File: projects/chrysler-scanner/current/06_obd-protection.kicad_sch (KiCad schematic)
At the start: 11 parts

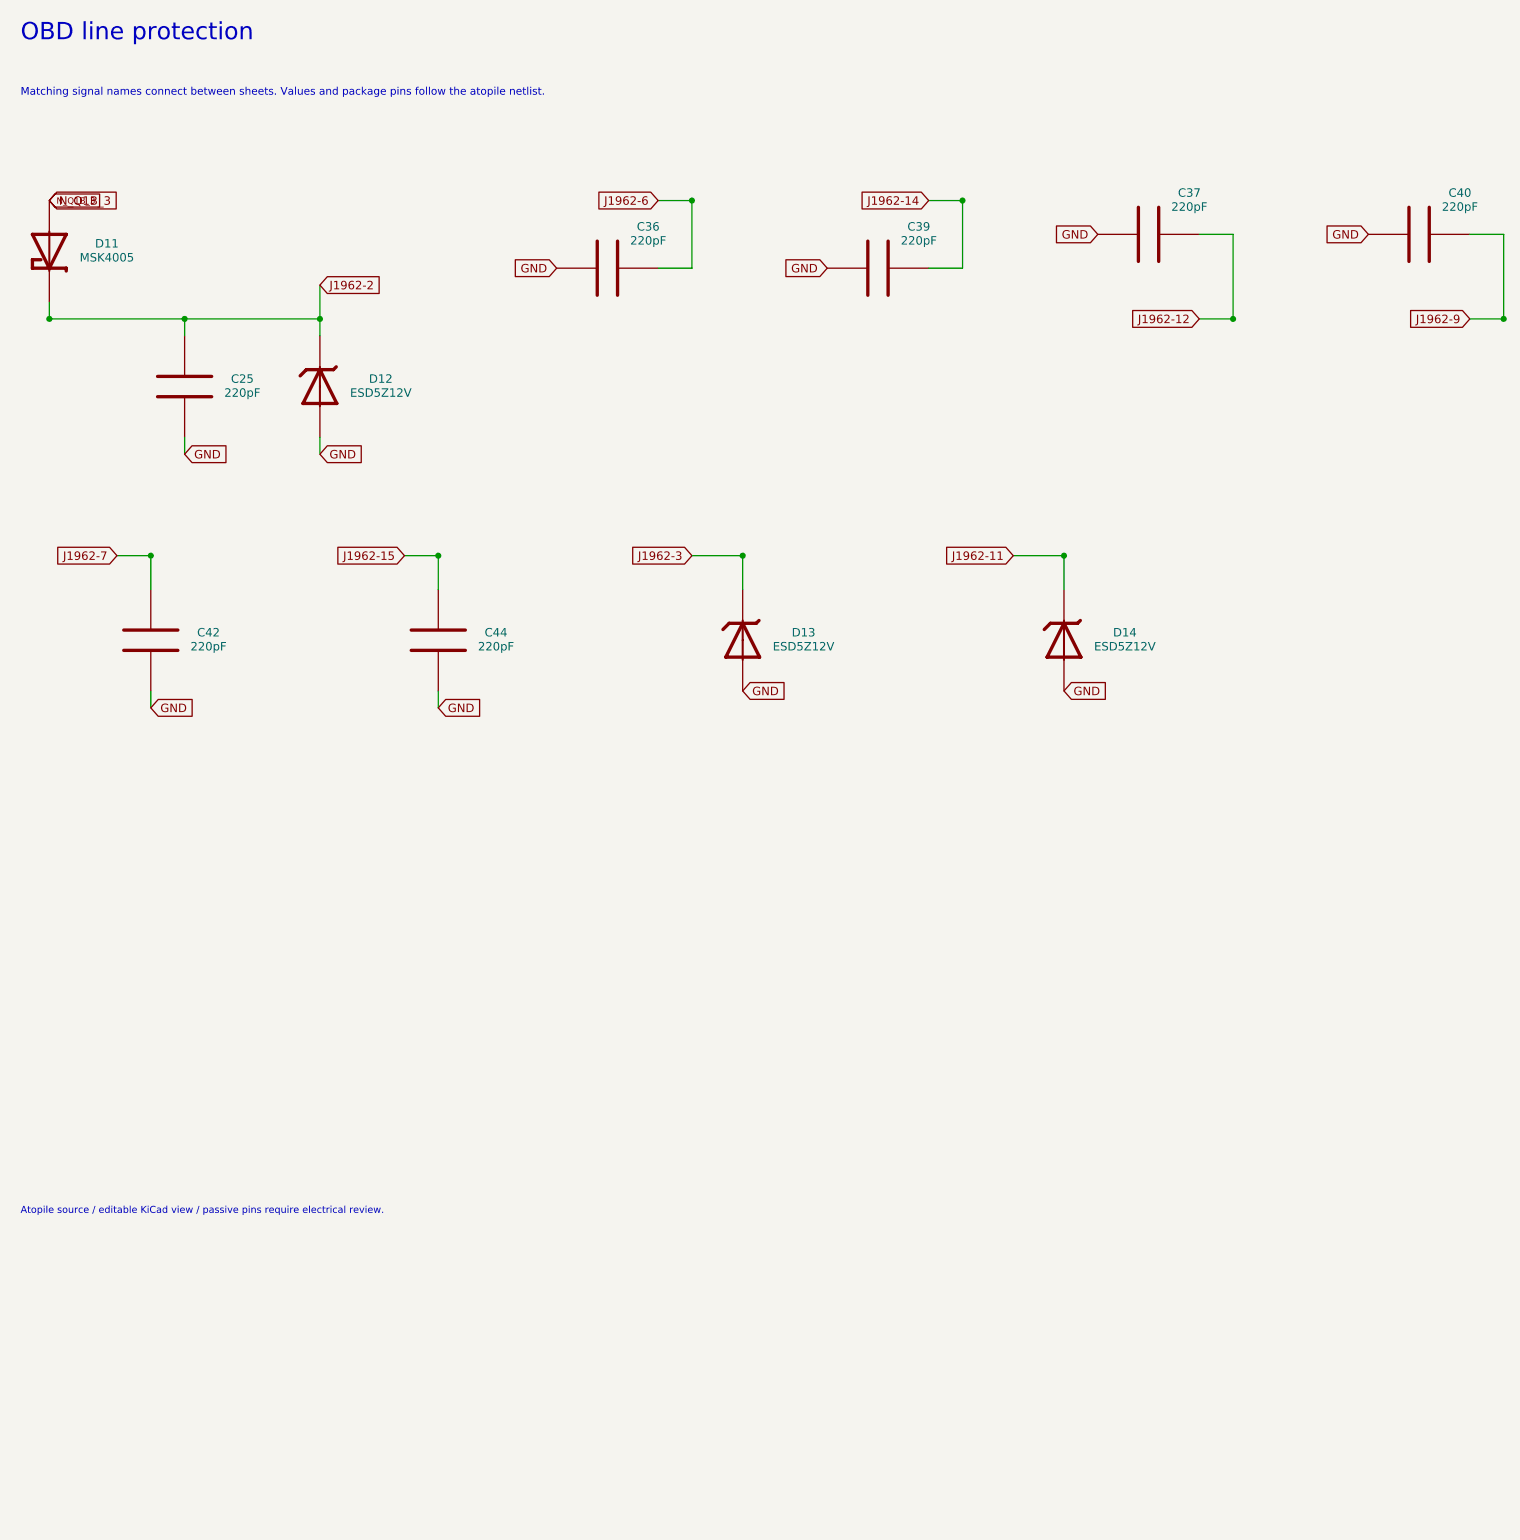
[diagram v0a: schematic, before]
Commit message: Finish scanner routing and add hierarchical system schematics
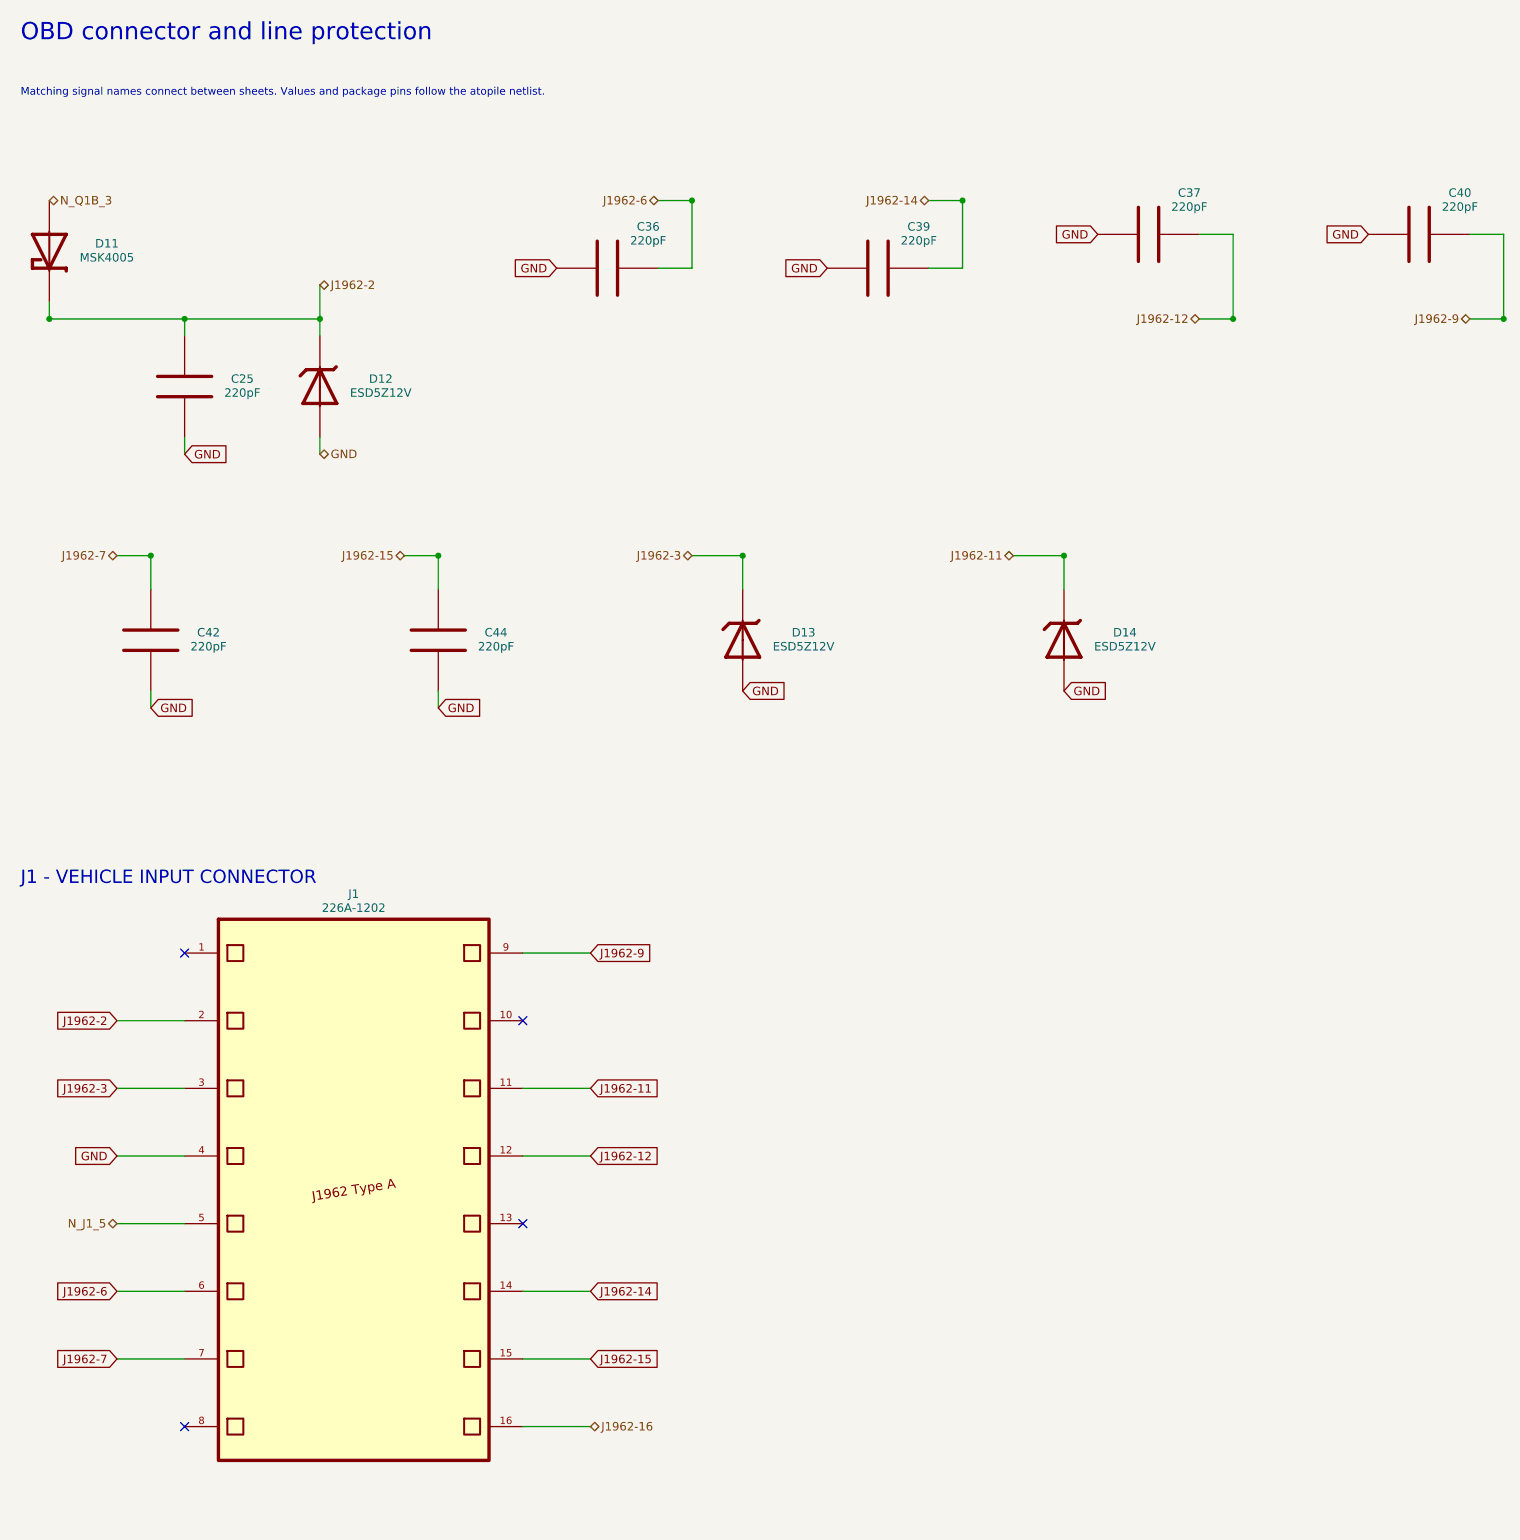
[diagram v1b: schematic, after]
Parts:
- added J1: 226A-1202, footprints:OBDII_ATTEND_226A-1202, symbol ChryslerScanner:J1
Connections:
- net GND: now also J1.4
- net J1962-11: now also J1.11
- net J1962-12: now also J1.12
- net J1962-14: now also J1.14
- net J1962-15: now also J1.15
- net J1962-2: now also J1.2
- net J1962-3: now also J1.3
- net J1962-6: now also J1.6
- net J1962-7: now also J1.7
- net J1962-9: now also J1.9
- new net J1962-16: J1.16
- new net N_J1_5: J1.5
- no-connect marks 0 -> 4
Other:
- note added: "J1 - VEHICLE INPUT CONNECTOR"
- note added: "OBD connector and line protection"
- note removed: "Atopile source / editable KiCad view / passive pins require electrical review."
- note removed: "OBD line protection"
- title: OBD line protection -> OBD connector and line protection

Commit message: Fix scanner protection, ADC isolation and health watchdog
Coordinate the bounded 12 V input clamp and programming FET/capacitor ratings, add powered-off ADC isolation, and supervise the AW9523B permit with a dedicated GPIO13 health heartbeat. Preserve original placements and document all deliberate source-PDF deviations.

Validation: native ERC and full DRC/parity/refill report zero findings; strict preservation/connectivity audit and final adversarial review pass within the documented prototype bounds. Regenerate Rev C PDF, BOM, manufacturing exports, processing sites and verified portable archives. Compatible firmware and bench/mechanical qualification remain required.
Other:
- moved on the sheet: C36, C37, C39, C40

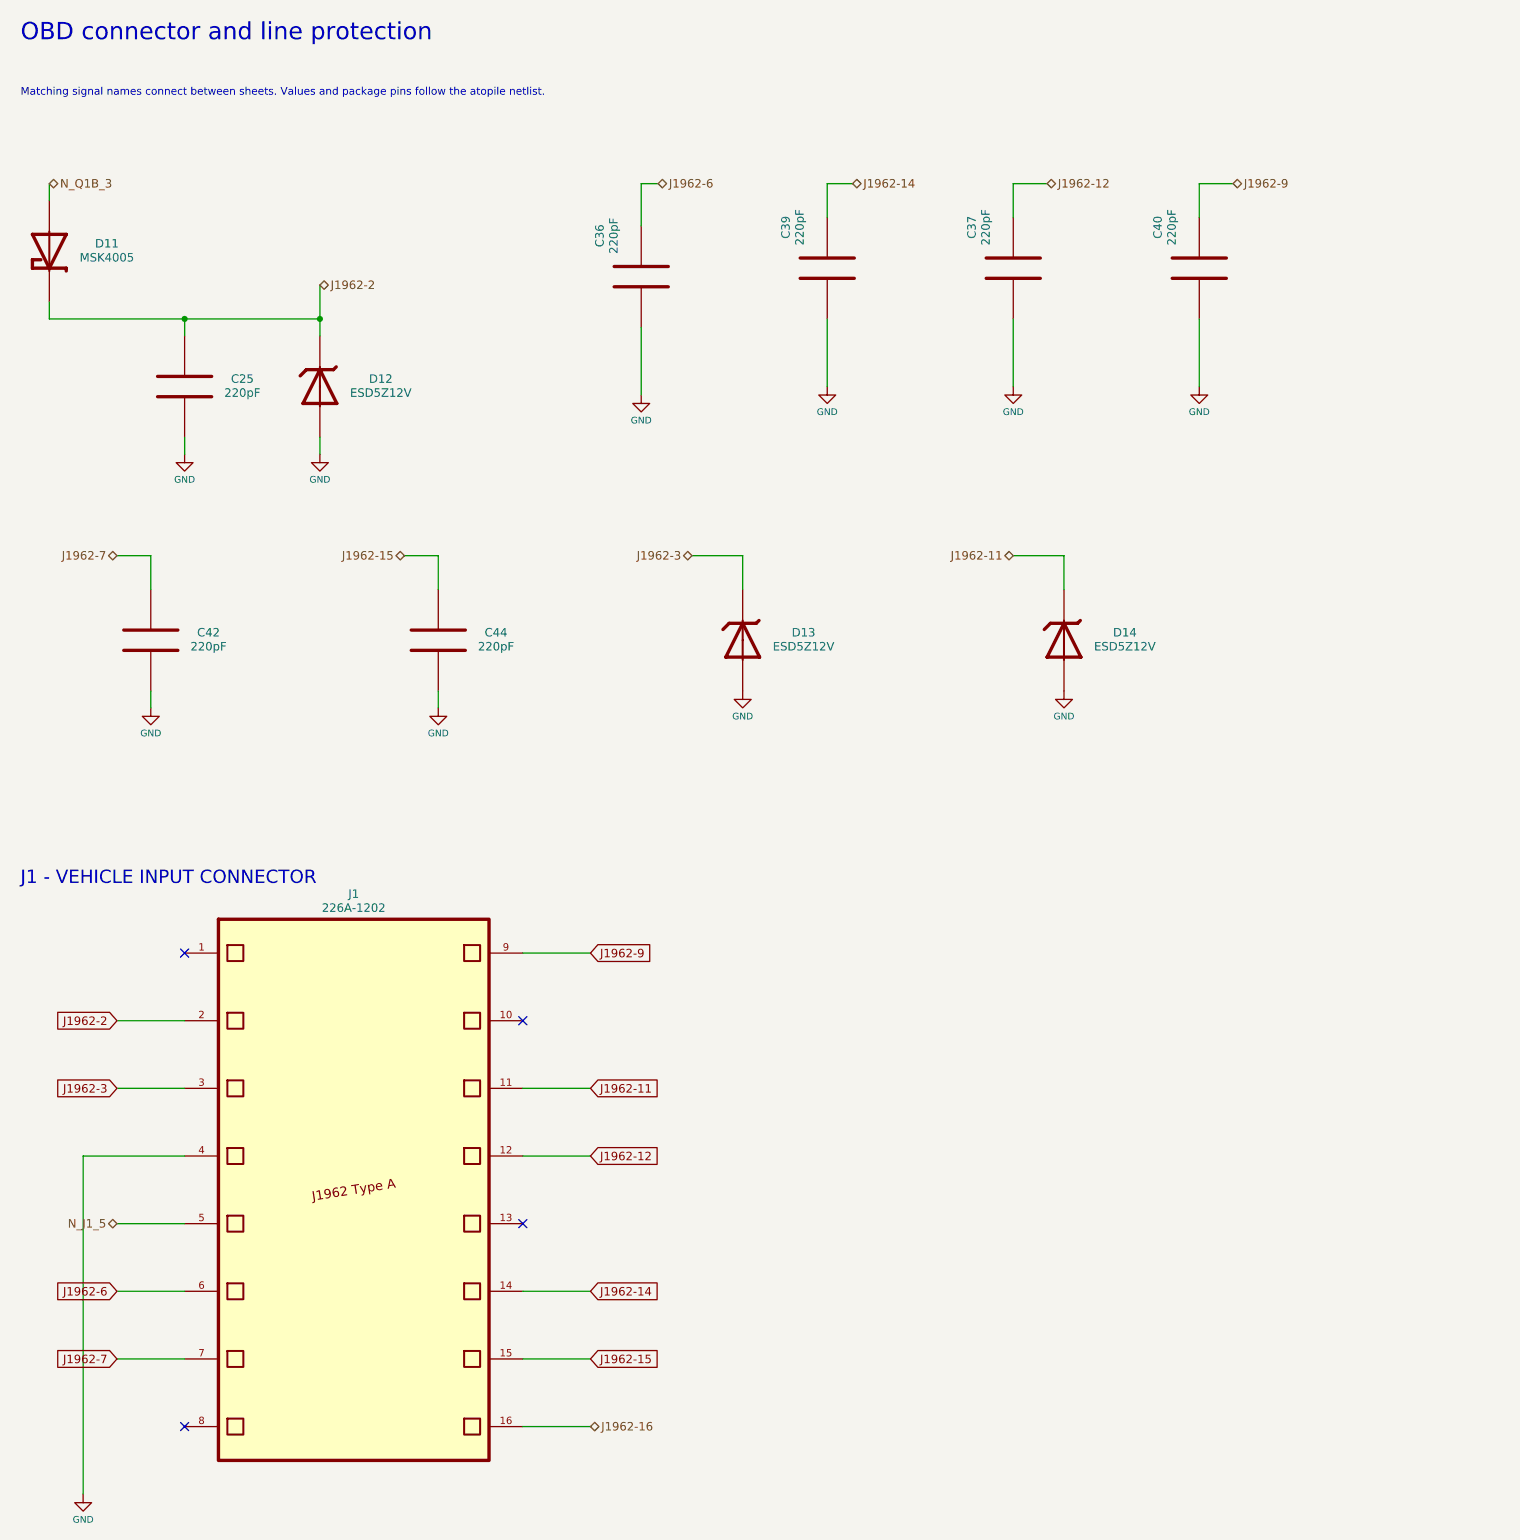
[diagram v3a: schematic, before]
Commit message: Group protection capacitors and document OBD mounting clearance
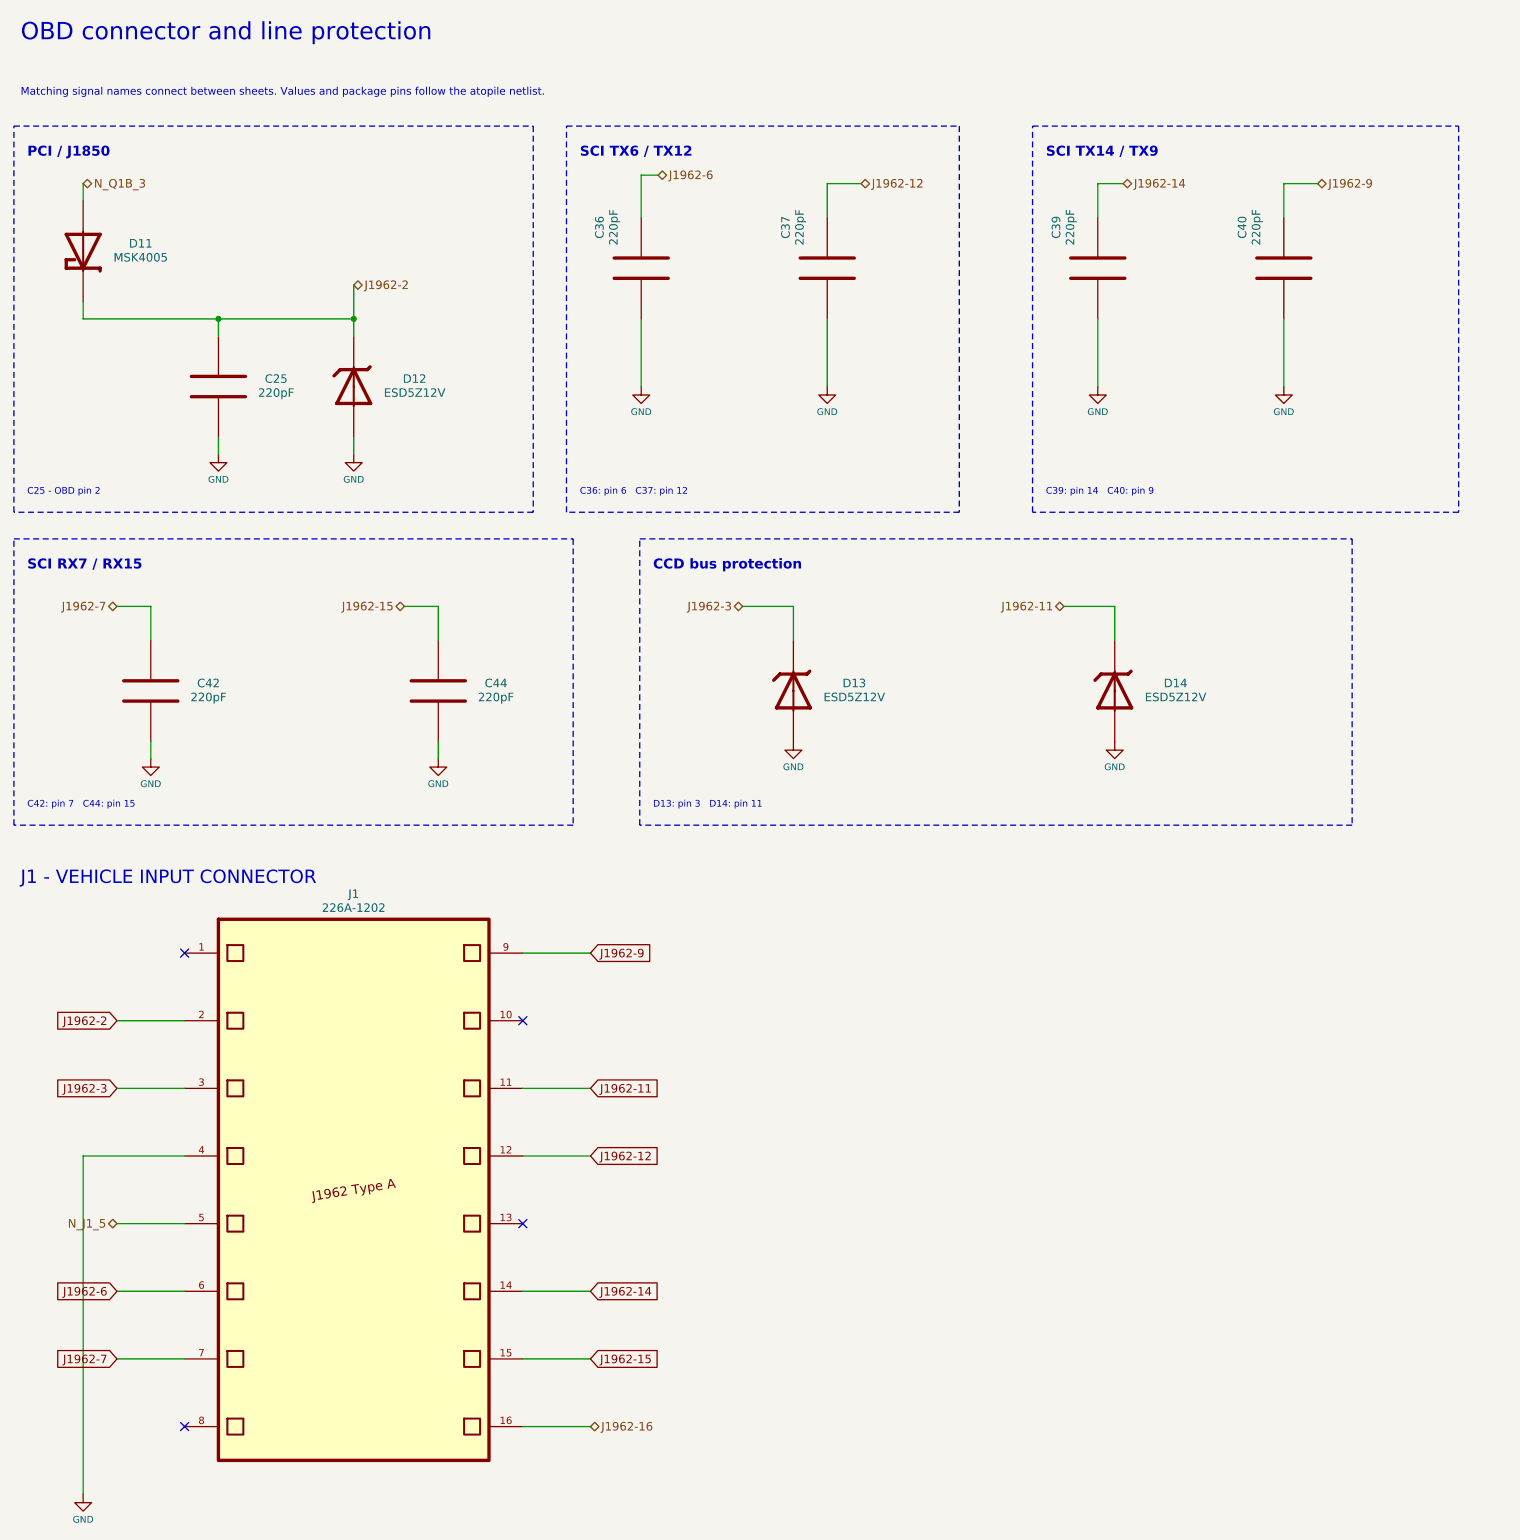
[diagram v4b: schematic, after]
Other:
- note added: "C25 - OBD pin 2"
- note added: "C36: pin 6 C37: pin 12"
- note added: "C39: pin 14 C40: pin 9"
- note added: "C42: pin 7 C44: pin 15"
- note added: "CCD bus protection"
- note added: "D13: pin 3 D14: pin 11"
- note added: "PCI / J1850"
- note added: "SCI RX7 / RX15"
- note added: "SCI TX14 / TX9"
- note added: "SCI TX6 / TX12"
- moved on the sheet: C25, C36, C37, C39, C40, C42, C44, D11, D12, D13, D14
